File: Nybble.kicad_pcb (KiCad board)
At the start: 2 copper layers, 106 parts, among them J1 USB_mini_micro_B, SW1 SW_PUSH, U1 ATMEGA32U4, X1 XTAL_GND

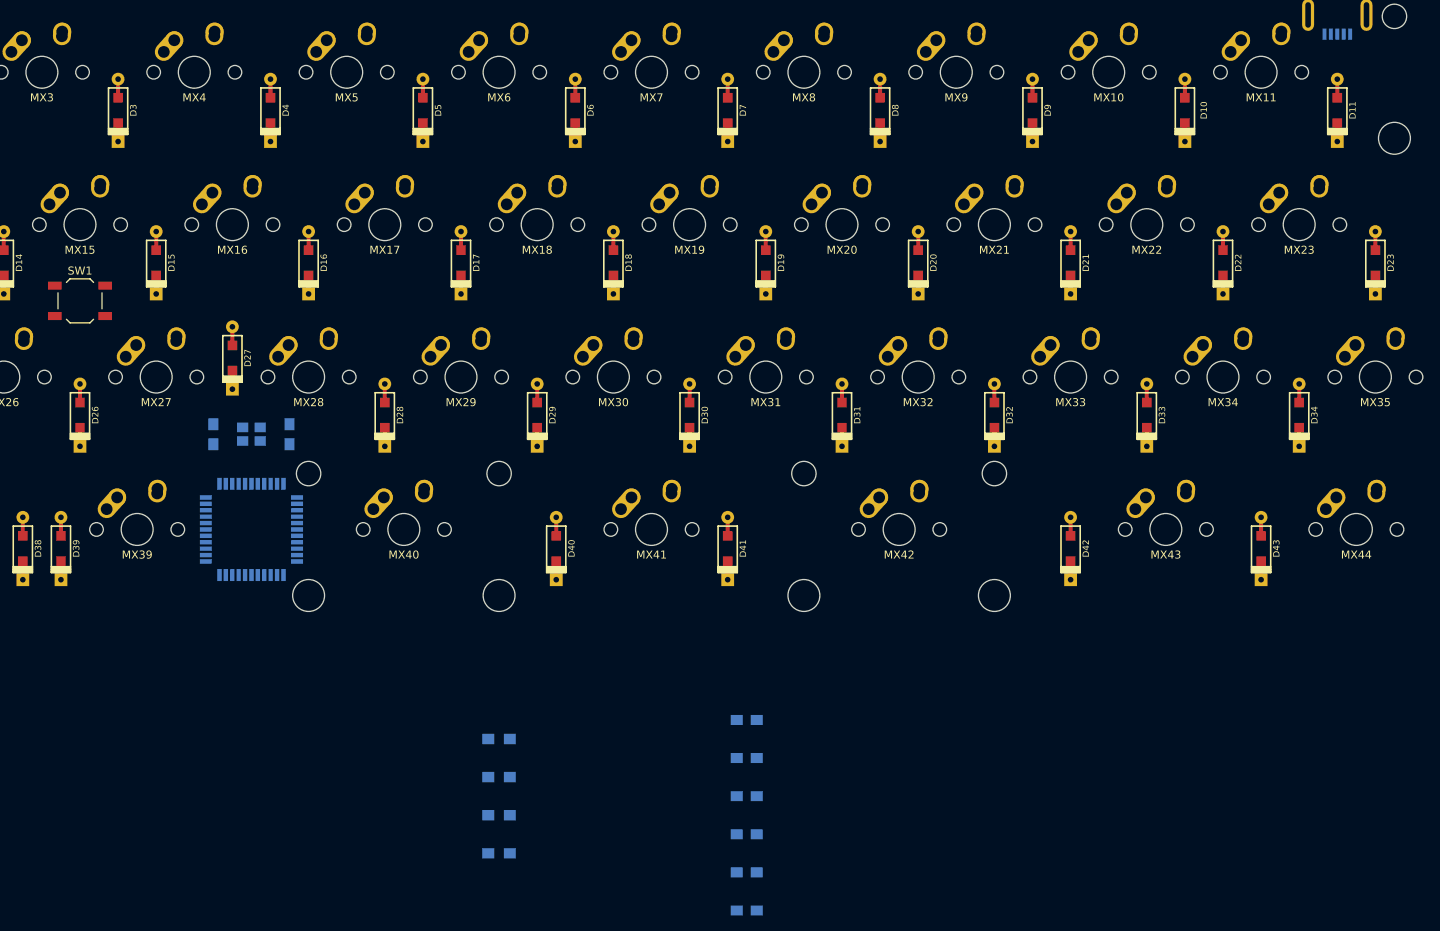
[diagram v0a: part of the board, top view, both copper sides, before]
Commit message: Got a draft of the component layout
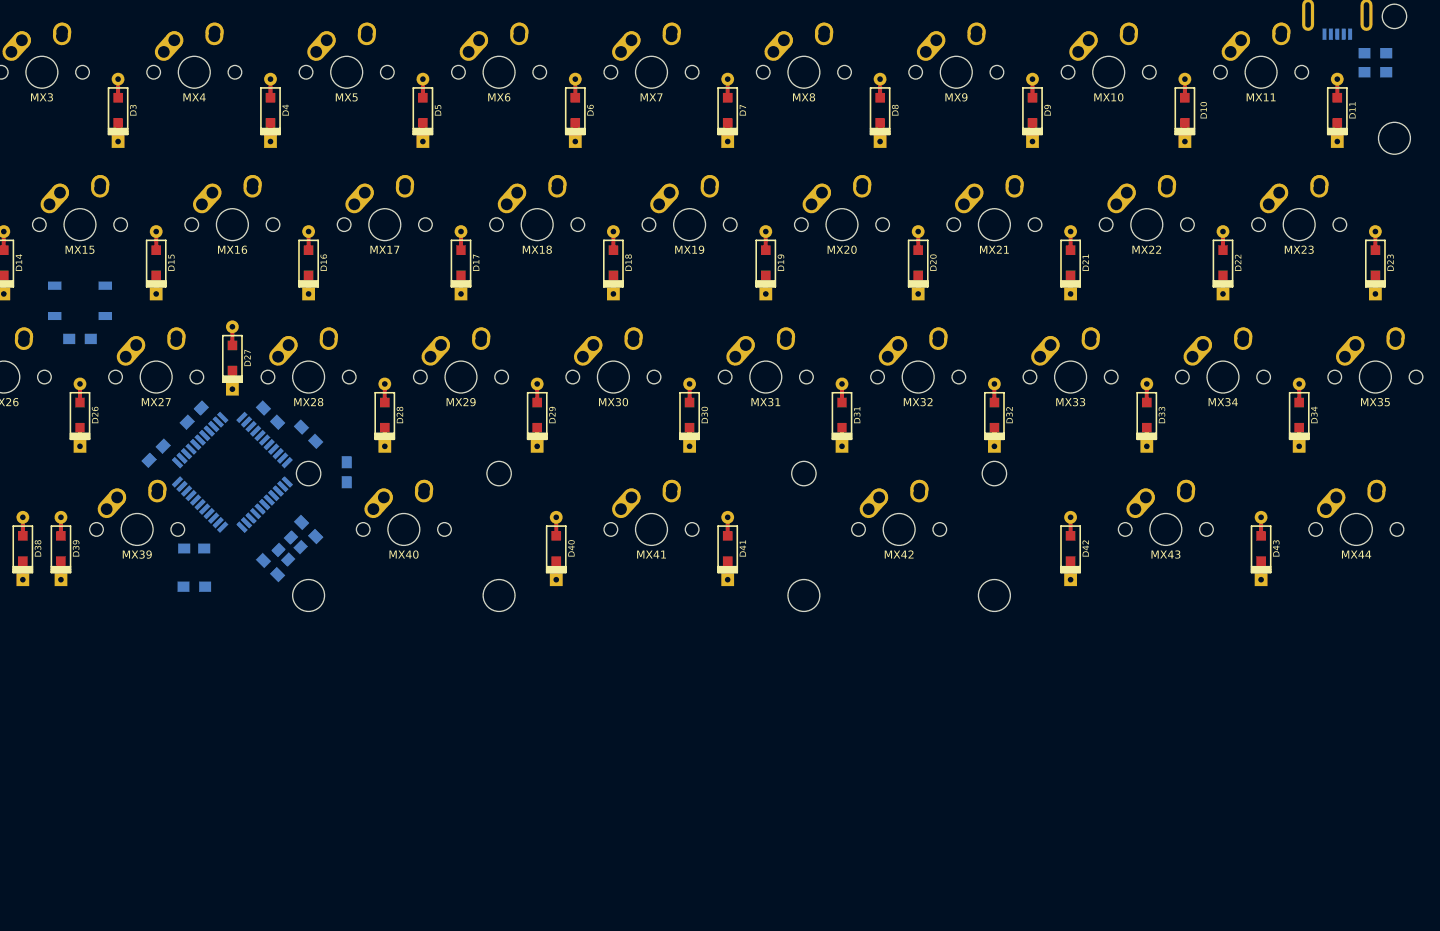
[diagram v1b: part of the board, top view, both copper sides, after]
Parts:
- SW1: moved to B.Cu
- moved R4 148.3 mm to (231.0, 26.2), turned to 180 degrees
- moved R3 143.6 mm to (231.0, 28.6), turned to 180 degrees
- moved C7 89.6 mm to (83.3, 71.4), turned to 45 degrees
- moved C8 85.9 mm to (92.9, 71.4), turned to 135 degrees
- moved C3 81.0 mm to (78.6, 76.2), turned to 45 degrees
- moved C6 77.7 mm to (83.3, 88.1)
- moved R1 72.4 mm to (69.1, 61.9)
- moved C4 68.1 mm to (97.6, 73.8), turned to 135 degrees
- moved C5 64.3 mm to (102.4, 78.6), turned to 270 degrees
- moved R2 44.9 mm to (83.3, 92.9)
- moved C1 18.1 mm to (92.9, 90.5), turned to 315 degrees
- moved X1 15.1 mm to (95.2, 88.1), turned to 45 degrees
- moved C2 12.1 mm to (97.6, 85.7), turned to 315 degrees
- moved U1 7.53 mm to (88.1, 78.6), turned to 225 degrees

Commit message: Made a few fine edits to the controller
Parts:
- moved R3 2.37 mm to (231.6, 30.9)
- moved C4 1.96 mm to (95.7, 74.3)
- moved R4 1.74 mm to (231.6, 27.8)
- moved C8 0.63 mm to (92.4, 71.0)
- moved J1 0.58 mm to (226.2, 24.4)
- moved U1 0.26 mm to (88.4, 78.6)
- moved R2 0.07 mm to (83.3, 92.8)
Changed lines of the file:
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@@
     (aux_axis_origin 0 0)
     (grid_origin 145.25625 85.725)
-    (visible_elements 7FFFE7FF)
+    (visible_elements 7FFFF7FF)
     (pcbplotparams
       (layerselection 0x00030_80000001)
@@
   )
   (module Capacitors_SMD:C_0805_HandSoldering (layer B.Cu)
-    (at 97.63125 73.81875 135)
+    (at 95.72625 74.295 135)
     (descr "Capacitor SMD 0805, hand soldering")
     (tags "capacitor 0805")
@@
   )
   (module Capacitors_SMD:C_0805_HandSoldering (layer B.Cu)
-    (at 92.86875 71.4375 135)
+    (at 92.42425 70.993 135)
     (descr "Capacitor SMD 0805, hand soldering")
     (tags "capacitor 0805")
@@
   )
   (module keyboard_parts:USB_miniB_hirose_5S8 (layer B.Cu)
-    (at 226.21875 23.8125)
+    (at 226.15525 24.384)
     (descr "USB miniB hirose UX60SC-MB-5S8")
     (tags "USB miniB hirose through hole UX60SC-MB-5S8")
@@
   )
   (module Resistors_SMD:R_0805_HandSoldering (layer B.Cu)
-    (at 83.34375 92.86875)
+    (at 83.28025 92.837)
     (descr "Resistor SMD 0805, hand soldering")
     (tags "resistor 0805")
@@
   )
   (module Resistors_SMD:R_0805_HandSoldering (layer B.Cu)
-    (at 230.98125 28.575 180)
+    (at 231.61625 30.861 180)
     (descr "Resistor SMD 0805, hand soldering")
     (tags "resistor 0805")
@@
   )
   (module Resistors_SMD:R_0805_HandSoldering (layer B.Cu)
-    (at 230.98125 26.19375 180)
+    (at 231.61625 27.813 180)
     (descr "Resistor SMD 0805, hand soldering")
     (tags "resistor 0805")
@@
   )
   (module Housings_QFP:TQFP-44_10x10mm_Pitch0.8mm (layer B.Cu)
-    (at 88.10625 78.58125 225)
+    (at 88.36025 78.613 225)
     (descr "44-Lead Plastic Thin Quad Flatpack (PT) - 10x10x1.0 mm Body [TQFP] (see Microchip Packaging Specification 00000049BS.pdf)")
     (tags "QFP 0.8")

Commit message: Created PCB edge
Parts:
- moved J1 0.65 mm to (226.3, 23.7)
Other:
- board outline added: 250.4 x 79 mm
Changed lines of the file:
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@@
     (area 16.393749 14.4433 265.23375 96.1739)
     (thickness 1.6)
-    (drawings 0)
+    (drawings 10)
     (tracks 0)
     (zones 0)
@@
   )
   (module keyboard_parts:USB_miniB_hirose_5S8 (layer B.Cu)
-    (at 226.15525 24.384)
+    (at 226.28225 23.749)
     (descr "USB miniB hirose UX60SC-MB-5S8")
     (tags "USB miniB hirose through hole UX60SC-MB-5S8")
@@
     )
   )
+  (gr_line (start 16.47825 96.647) (end 16.73225 96.647) (angle 90) (layer Edge.Cuts) (width 0.1))
+  (gr_arc (start 16.47825 95.377) (end 16.47825 96.647) (angle 90) (layer Edge.Cuts) (width 0.1))
+  (gr_line (start 264.38225 96.647) (end 16.73225 96.647) (angle 90) (layer Edge.Cuts) (width 0.1))
+  (gr_arc (start 264.38225 95.377) (end 265.65225 95.377) (angle 90) (layer Edge.Cuts) (width 0.1))
+  (gr_line (start 265.65225 93.599) (end 265.65225 95.377) (angle 90) (layer Edge.Cuts) (width 0.1))
+  (gr_line (start 265.65225 19.177) (end 265.65225 93.599) (angle 90) (layer Edge.Cuts) (width 0.1))
+  (gr_line (start 15.20825 19.177) (end 15.20825 95.377) (angle 90) (layer Edge.Cuts) (width 0.1))
+  (gr_line (start 16.73225 17.653) (end 264.12825 17.653) (angle 90) (layer Edge.Cuts) (width 0.1))
+  (gr_arc (start 16.73225 19.177) (end 15.20825 19.177) (angle 90) (layer Edge.Cuts) (width 0.1))
+  (gr_arc (start 264.12825 19.177) (end 264.12825 17.653) (angle 90) (layer Edge.Cuts) (width 0.1))
 )

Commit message: Added Ground zones
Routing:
- added copper zone on B.Cu, net GND
- added copper zone on F.Cu, net GND
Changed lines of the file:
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@@
     (aux_axis_origin 0 0)
     (grid_origin 145.25625 85.725)
-    (visible_elements 7FFFF7FF)
+    (visible_elements 7FFFE7FF)
     (pcbplotparams
       (layerselection 0x00030_80000001)
@@
   (gr_arc (start 16.73225 19.177) (end 15.20825 19.177) (angle 90) (layer Edge.Cuts) (width 0.1))
   (gr_arc (start 264.12825 19.177) (end 264.12825 17.653) (angle 90) (layer Edge.Cuts) (width 0.1))
+  (zone (net 2) (net_name GND) (layer F.Cu) (hatch edge 0.508)
+    (connect_pads (clearance 0.508))
+    (min_thickness 0.254)
+    (fill (arc_segments 16) (thermal_gap 0.508) (thermal_bridge_width 0.508))
+    (polygon
+      (pts
+        (xy 15.20825 95.377) (xy 15.20825 96.647) (xy 265.65225 96.647) (xy 265.65225 17.653) (xy 15.20825 17.653)
+      )
+    )
+  )
+  (zone (net 2) (net_name GND) (layer B.Cu) (hatch edge 0.508)
+    (connect_pads (clearance 0.508))
+    (min_thickness 0.254)
+    (fill (arc_segments 16) (thermal_gap 0.508) (thermal_bridge_width 0.508))
+    (polygon
+      (pts
+        (xy 15.20825 95.377) (xy 15.20825 96.647) (xy 265.65225 96.647) (xy 265.65225 17.653) (xy 15.20825 17.653)
+      )
+    )
+  )
 )
